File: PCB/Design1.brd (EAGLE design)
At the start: 73 x 41 mm, 41 parts, among them J1 FTDI, U1 ATMEGA2560AU, Y1 16MHZ

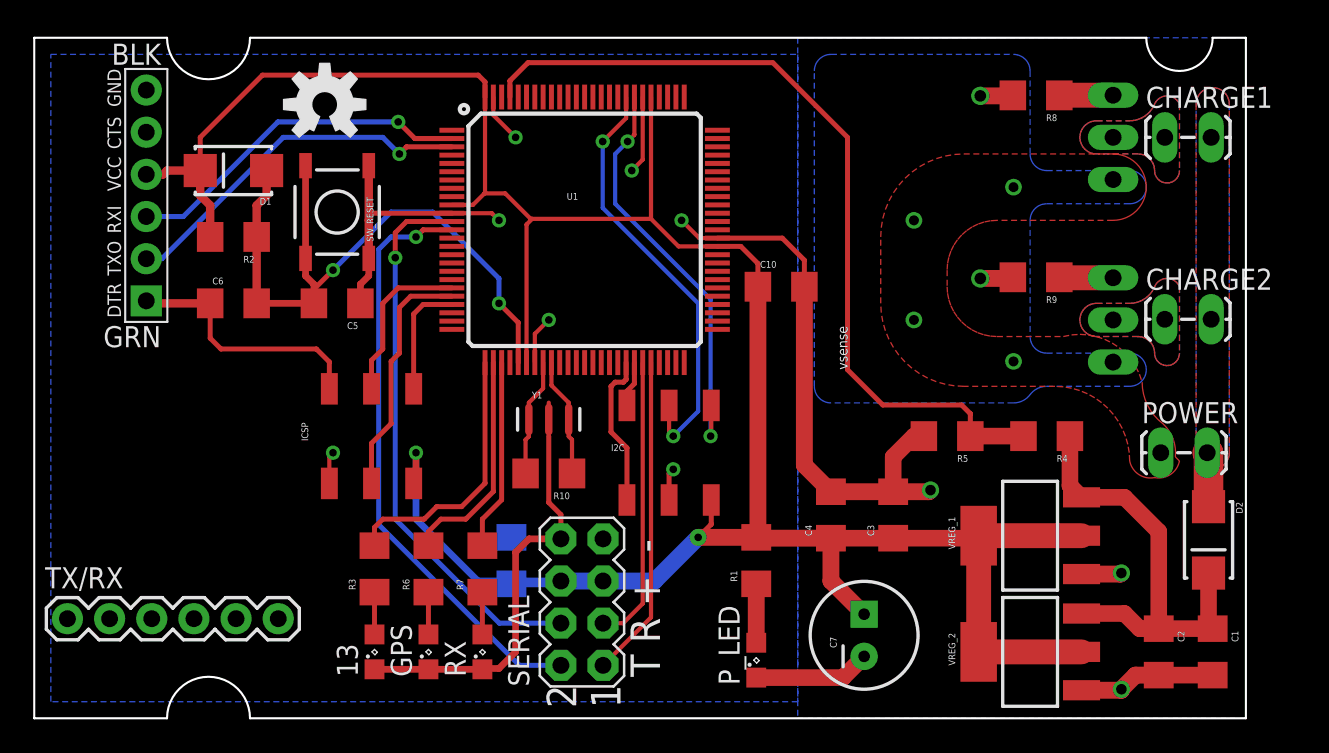
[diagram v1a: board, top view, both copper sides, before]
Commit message: Removed 1x 5v regulator; relabeling
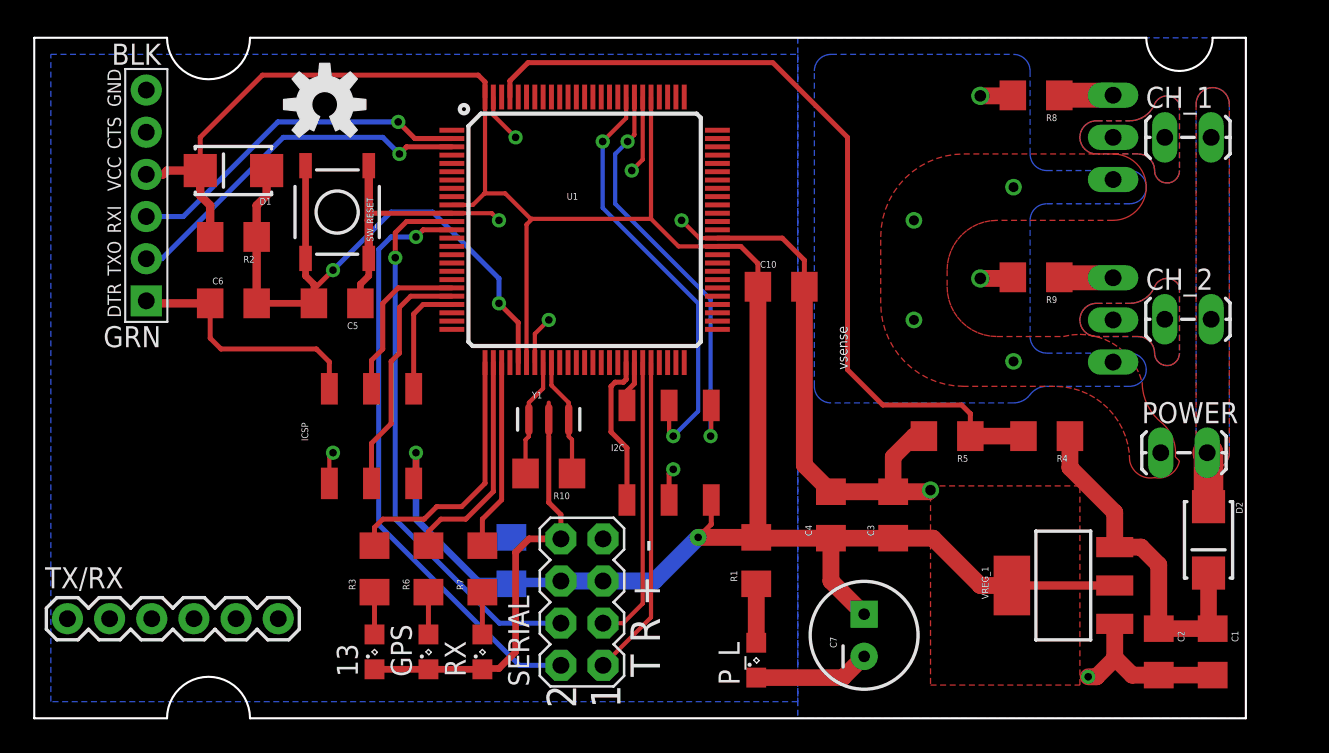
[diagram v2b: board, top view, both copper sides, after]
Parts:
- removed VREG_2: (no value), SparkFun-PowerIC:SOT223
- P_L: value red -> (none)
- moved VREG_1 3.61 mm to (62.0, 8.00)
- renumbered CHARGE1 to CH_1, CHARGE2 to CH_2, P_LED to P_L
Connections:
- net 5V: no longer VREG_2.2, VREG_2.4
- net GND: no longer VREG_2.1
- net VIN_RECTIFIED: no longer VREG_2.3
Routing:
- net 5V: track 161.3 -> 151.2 mm
- net VIN_RECTIFIED: track 27.1 -> 21.5 mm
- net GND: track 111.2 -> 111.0 mm, vias 16 -> 15
- added copper zone on layer 1, net 5V
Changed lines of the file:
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@@
 <text x="35.32" y="0.62" size="1.778" layer="21" rot="R90">2
 1</text>
-<dimension x1="74" y1="41" x2="74" y2="0" x3="78" y3="20.5" textsize="1.778" layer="51" visible="yes"/>
-<dimension x1="0" y1="42" x2="73" y2="42" x3="36.5" y3="43" textsize="1.778" layer="51" visible="yes"/>
 <wire x1="46" y1="41" x2="46" y2="18" width="0.254" layer="22"/>
 <wire x1="46" y1="18" x2="65" y2="18" width="0.254" layer="22"/>
@@
 <attribute name="VALUE" x="23.822" y="17.408" size="0.4064" layer="27" rot="R180"/>
 </element>
-<element name="P_LED" library="led" package="SML0805" value="red" x="43.5" y="3.5" rot="R90"/>
+<element name="P_L" library="led" package="SML0805" value="" x="43.5" y="3.5" rot="R90"/>
 <element name="R1" library="SparkFun-Resistors" package="1206" value="100Ω" x="43.5" y="9.5" rot="R90"/>
 <element name="GPS" library="led" package="SML0805" value="" x="23.75" y="4" rot="R90"/>
@@
 <element name="R8" library="SparkFun-Resistors" package="1206" value="10KΩ" x="60.36" y="37.53" rot="R180"/>
 <element name="R9" library="SparkFun-Resistors" package="1206" value="10KΩ" x="60.36" y="26.57" rot="R180"/>
-<element name="CHARGE1" library="SparkFun-Connectors" package="1X02_LOCK_LONGPADS" value="" x="68.24" y="35"/>
-<element name="CHARGE2" library="SparkFun-Connectors" package="1X02_LOCK_LONGPADS" value="" x="68.24" y="24.04"/>
-<element name="VREG_1" library="SparkFun-PowerIC" package="SOT223" value="" x="60" y="11" rot="R90">
-<attribute name="PROD_ID" value="VREG-08170" x="60" y="11" size="1.778" layer="27" rot="R90" display="off"/>
-</element>
-<element name="VREG_2" library="SparkFun-PowerIC" package="SOT223" value="" x="60" y="4" rot="R90">
-<attribute name="PROD_ID" value="VREG-08170" x="60" y="4" size="1.778" layer="27" rot="R90" display="off"/>
+<element name="CH_1" library="SparkFun-Connectors" package="1X02_LOCK_LONGPADS" value="" x="68.24" y="35"/>
+<element name="CH_2" library="SparkFun-Connectors" package="1X02_LOCK_LONGPADS" value="" x="68.24" y="24.04"/>
+<element name="VREG_1" library="SparkFun-PowerIC" package="SOT223" value="" x="62" y="8" rot="R90">
+<attribute name="PROD_ID" value="VREG-08170" x="62" y="8" size="1.778" layer="27" rot="R90" display="off"/>
 </element>
 <element name="C7" library="SparkFun-Capacitors" package="CPOL-RADIAL-100UF-25V" value="470uF" x="50" y="5" rot="R90"/>
@@
 <contactref element="R5" pad="2"/>
 <contactref element="ICSP" pad="6"/>
-<contactref element="P_LED" pad="C"/>
+<contactref element="P_L" pad="C"/>
 <contactref element="RX" pad="C"/>
 <contactref element="GPS" pad="C"/>
@@
 <contactref element="R8" pad="2"/>
 <contactref element="R9" pad="2"/>
-<contactref element="VREG_2" pad="1"/>
 <contactref element="VREG_1" pad="1"/>
 <contactref element="C7" pad="2"/>
@@
 <vertex x="73" y="41"/>
 </polygon>
-<via x="65.5" y="8.75" extent="1-16" drill="0.635"/>
-<via x="65.5" y="1.75" extent="1-16" drill="0.635"/>
 <wire x1="67.75" y1="2.6" x2="71" y2="2.6" width="1" layer="1"/>
 <wire x1="51.75" y1="13.65" x2="51.75" y2="15.75" width="1" layer="1"/>
@@
 <wire x1="53" y1="17" x2="53.6" y2="17" width="1" layer="1"/>
 <via x="54" y="13.75" extent="1-16" drill="0.635"/>
-<wire x1="63.0988" y1="1.6886" x2="65.5" y2="1.6886" width="1.016" layer="1"/>
-<wire x1="65.5" y1="1.6886" x2="65.5" y2="1.75" width="1.016" layer="1"/>
-<wire x1="67.75" y1="2.6" x2="66.35" y2="2.6" width="1.016" layer="1"/>
-<wire x1="66.35" y1="2.6" x2="65.5" y2="1.75" width="1.016" layer="1"/>
-<wire x1="63.0988" y1="8.6886" x2="65.4386" y2="8.6886" width="1.016" layer="1"/>
-<wire x1="65.4386" y1="8.6886" x2="65.5" y2="8.75" width="1.016" layer="1"/>
 <wire x1="51.75" y1="13.65" x2="53.9" y2="13.65" width="1.016" layer="1"/>
 <wire x1="53.9" y1="13.65" x2="54" y2="13.75" width="1.016" layer="1"/>
@@
 <wire x1="29" y1="10" x2="29.81" y2="10.81" width="0.4064" layer="1"/>
 <wire x1="29.81" y1="10.81" x2="31.73" y2="10.81" width="0.4064" layer="1"/>
+<wire x1="67.75" y1="2.6" x2="66.15" y2="2.6" width="1.016" layer="1"/>
+<wire x1="66.15" y1="2.6" x2="65.125" y2="3.625" width="1.016" layer="1"/>
+<wire x1="65.125" y1="3.625" x2="65.0988" y2="3.6512" width="1.016" layer="1"/>
+<wire x1="65.0988" y1="3.6512" x2="65.0988" y2="5.6886" width="1.016" layer="1"/>
+<via x="63.5" y="2.5" extent="1-16" drill="0.4572"/>
+<wire x1="63.5" y1="2.5" x2="64" y2="2.5" width="1.016" layer="1"/>
+<wire x1="64" y1="2.5" x2="65.125" y2="3.625" width="1.016" layer="1"/>
 </signal>
 <signal name="RESET">
@@
 <contactref element="VREG_1" pad="2"/>
 <contactref element="VREG_1" pad="4"/>
-<contactref element="VREG_2" pad="2"/>
-<contactref element="VREG_2" pad="4"/>
 <contactref element="C7" pad="1"/>
-<wire x1="63.0988" y1="11" x2="56.901" y2="11" width="1.5" layer="1"/>
-<wire x1="63.0988" y1="4" x2="56.901" y2="4" width="1.5" layer="1"/>
-<wire x1="56.901" y1="11" x2="56.901" y2="4" width="1.5" layer="1"/>
 <wire x1="48" y1="10.85" x2="51.75" y2="10.85" width="1" layer="1"/>
-<wire x1="51.75" y1="10.85" x2="56.751" y2="10.85" width="1" layer="1"/>
-<wire x1="56.751" y1="10.85" x2="56.901" y2="11" width="1" layer="1"/>
 <contactref element="C9" pad="1"/>
 <contactref element="C10" pad="1"/>
@@
 <wire x1="28.75" y1="8.1" x2="31.56" y2="8.1" width="0.4064" layer="16"/>
 <wire x1="31.56" y1="8.1" x2="31.73" y2="8.27" width="0.4064" layer="16"/>
+<polygon width="0.3" layer="1" isolate="1.016">
+<vertex x="54" y="14"/>
+<vertex x="54" y="2"/>
+<vertex x="63" y="2"/>
+<vertex x="63" y="14"/>
+</polygon>
+<wire x1="51.75" y1="10.85" x2="54.15" y2="10.85" width="1.016" layer="1"/>
+<wire x1="54.15" y1="10.85" x2="57" y2="8" width="1.016" layer="1"/>
+<wire x1="57" y1="8" x2="58.901" y2="8" width="1.016" layer="1"/>
+<wire x1="65.0988" y1="8" x2="58.901" y2="8" width="0.508" layer="1"/>
 </signal>
 <signal name="TX1">
@@
 <contactref element="POWER" pad="2"/>
 <contactref element="D2" pad="A"/>
-<contactref element="CHARGE2" pad="2"/>
-<contactref element="CHARGE1" pad="2"/>
+<contactref element="CH_2" pad="2"/>
+<contactref element="CH_1" pad="2"/>
 <polygon width="0.254" layer="16" isolate="0.254" thermals="no">
 <vertex x="71" y="38" curve="-90"/>
@@
 </signal>
 <signal name="N$2">
-<contactref element="P_LED" pad="A"/>
+<contactref element="P_L" pad="A"/>
 <contactref element="R1" pad="1"/>
 <wire x1="43.5" y1="4.55" x2="43.5" y2="8.1" width="1.016" layer="1"/>
@@
 <signal name="MOS1">
 <contactref element="MOS1" pad="2"/>
-<contactref element="CHARGE1" pad="1"/>
+<contactref element="CH_1" pad="1"/>
 <polygon width="0.254" layer="16" thermals="no">
 <vertex x="64" y="36"/>
@@
 <signal name="MOS2">
 <contactref element="MOS2" pad="2"/>
-<contactref element="CHARGE2" pad="1"/>
+<contactref element="CH_2" pad="1"/>
 <polygon width="0.254" layer="1" thermals="no">
 <vertex x="64" y="25"/>
@@
 <contactref element="C1" pad="1"/>
 <contactref element="VREG_1" pad="3"/>
-<contactref element="VREG_2" pad="3"/>
 <wire x1="71" y1="5.4" x2="67.75" y2="5.4" width="1" layer="1"/>
 <wire x1="71" y1="5.4" x2="70.75" y2="5.65" width="1" layer="1"/>
 <wire x1="70.75" y1="5.65" x2="70.75" y2="8.75" width="1" layer="1"/>
-<wire x1="63.0988" y1="13.3114" x2="65.6886" y2="13.3114" width="1" layer="1"/>
-<wire x1="65.6886" y1="13.3114" x2="67.75" y2="11.25" width="1" layer="1"/>
-<wire x1="67.75" y1="11.25" x2="67.75" y2="5.4" width="1" layer="1"/>
-<wire x1="63.0988" y1="6.3114" x2="65.6886" y2="6.3114" width="1" layer="1"/>
-<wire x1="65.6886" y1="6.3114" x2="66.6" y2="5.4" width="1" layer="1"/>
-<wire x1="66.6" y1="5.4" x2="67.75" y2="5.4" width="1" layer="1"/>
-<wire x1="63.0988" y1="13.3114" x2="62.4" y2="14.0102" width="1" layer="1"/>
-<wire x1="62.4" y1="14.0102" x2="62.4" y2="17" width="1" layer="1"/>
+<wire x1="67.75" y1="5.4" x2="67.75" y2="9.25" width="1.016" layer="1"/>
+<wire x1="67.75" y1="9.25" x2="66.6886" y2="10.3114" width="1.016" layer="1"/>
+<wire x1="66.6886" y1="10.3114" x2="65.0988" y2="10.3114" width="1.016" layer="1"/>
+<wire x1="62.4" y1="17" x2="62.4" y2="15.1" width="1.016" layer="1"/>
+<wire x1="62.4" y1="15.1" x2="65.0988" y2="12.4012" width="1.016" layer="1"/>
+<wire x1="65.0988" y1="12.4012" x2="65.0988" y2="10.3114" width="1.016" layer="1"/>
 </signal>
 <signal name="N$5">

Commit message: Labeling Cleanup
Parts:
- ATMEGA2560AU: value ATMEGA2560AU -> (none)
- renumbered U1 to ATMEGA2560AU, VREG_1 to VREG
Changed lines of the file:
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@@
 </autorouter>
 <elements>
-<element name="U1" library="SparkFun-DigitalIC" package="TQFP100" value="ATMEGA2560AU" x="33.16" y="29.43" locked="yes" smashed="yes">
+<element name="ATMEGA2560AU" library="SparkFun-DigitalIC" package="TQFP100" value="" x="33.16" y="29.43" locked="yes">
 <attribute name="PROD_ID" value="IC-10040" x="33.16" y="29.43" size="1.778" layer="27" display="off"/>
-<attribute name="NAME" x="32.08" y="31.24" size="0.4064" layer="25"/>
-<attribute name="VALUE" x="31.08" y="26.62" size="0.4064" layer="27"/>
 </element>
 <element name="J1" library="SparkFun-Connectors" package="FTDI_DEVICE_SIDE" value="FTDI" x="6.75" y="31.5" locked="yes" rot="R90"/>
@@
 <element name="CH_1" library="SparkFun-Connectors" package="1X02_LOCK_LONGPADS" value="" x="68.24" y="35"/>
 <element name="CH_2" library="SparkFun-Connectors" package="1X02_LOCK_LONGPADS" value="" x="68.24" y="24.04"/>
-<element name="VREG_1" library="SparkFun-PowerIC" package="SOT223" value="" x="62" y="8" rot="R90">
+<element name="VREG" library="SparkFun-PowerIC" package="SOT223" value="" x="62" y="8" rot="R90">
 <attribute name="PROD_ID" value="VREG-08170" x="62" y="8" size="1.778" layer="27" rot="R90" display="off"/>
 </element>
@@
 <signals>
 <signal name="GND">
-<contactref element="U1" pad="81"/>
-<contactref element="U1" pad="62"/>
+<contactref element="ATMEGA2560AU" pad="81"/>
+<contactref element="ATMEGA2560AU" pad="62"/>
 <contactref element="J1" pad="P$6"/>
 <contactref element="J1" pad="P$5"/>
 <contactref element="13" pad="C"/>
 <contactref element="POWER" pad="1"/>
-<contactref element="U1" pad="32"/>
-<contactref element="U1" pad="11"/>
-<contactref element="U1" pad="99"/>
+<contactref element="ATMEGA2560AU" pad="32"/>
+<contactref element="ATMEGA2560AU" pad="11"/>
+<contactref element="ATMEGA2560AU" pad="99"/>
 <contactref element="C5" pad="1"/>
 <contactref element="C1" pad="2"/>
@@
 <contactref element="R8" pad="2"/>
 <contactref element="R9" pad="2"/>
-<contactref element="VREG_1" pad="1"/>
+<contactref element="VREG" pad="1"/>
 <contactref element="C7" pad="2"/>
 <polygon width="0.254" layer="16" isolate="1.016" thermals="no" rank="2">
@@
 <contactref element="SW_RESET" pad="3"/>
 <contactref element="SW_RESET" pad="4"/>
-<contactref element="U1" pad="30"/>
+<contactref element="ATMEGA2560AU" pad="30"/>
 <wire x1="13.4" y1="25" x2="13.4" y2="29" width="0.508" layer="1"/>
 <wire x1="13.4" y1="29" x2="13.4" y2="30.9" width="0.508" layer="1"/>
@@
 <signal name="LED_13">
 <contactref element="R3" pad="2"/>
-<contactref element="U1" pad="26"/>
+<contactref element="ATMEGA2560AU" pad="26"/>
 <wire x1="27.16" y1="21.43" x2="27.16" y2="14.16" width="0.3" layer="1"/>
 <wire x1="27.16" y1="14.16" x2="25.75" y2="12.75" width="0.3" layer="1"/>
@@
 </signal>
 <signal name="TX0">
-<contactref element="U1" pad="3"/>
+<contactref element="ATMEGA2560AU" pad="3"/>
 <contactref element="J1" pad="P$2"/>
 <wire x1="6.75" y1="27.69" x2="7.69" y2="27.69" width="0.3048" layer="16"/>
@@
 </signal>
 <signal name="RX0">
-<contactref element="U1" pad="2"/>
+<contactref element="ATMEGA2560AU" pad="2"/>
 <contactref element="J1" pad="P$3"/>
 <via x="21.93" y="35.93" extent="1-16" drill="0.4572"/>
@@
 </signal>
 <signal name="5V">
-<contactref element="U1" pad="10"/>
-<contactref element="U1" pad="80"/>
-<contactref element="U1" pad="61"/>
-<contactref element="U1" pad="31"/>
-<contactref element="U1" pad="100"/>
+<contactref element="ATMEGA2560AU" pad="10"/>
+<contactref element="ATMEGA2560AU" pad="80"/>
+<contactref element="ATMEGA2560AU" pad="61"/>
+<contactref element="ATMEGA2560AU" pad="31"/>
+<contactref element="ATMEGA2560AU" pad="100"/>
 <contactref element="J1" pad="P$4"/>
 <contactref element="C4" pad="1"/>
@@
 <contactref element="ICSP" pad="2"/>
 <contactref element="R1" pad="2"/>
-<contactref element="VREG_1" pad="2"/>
-<contactref element="VREG_1" pad="4"/>
+<contactref element="VREG" pad="2"/>
+<contactref element="VREG" pad="4"/>
 <contactref element="C7" pad="1"/>
 <wire x1="48" y1="10.85" x2="51.75" y2="10.85" width="1" layer="1"/>
@@
 </signal>
 <signal name="TX1">
-<contactref element="U1" pad="46"/>
+<contactref element="ATMEGA2560AU" pad="46"/>
 <contactref element="SERIAL" pad="1"/>
 <wire x1="37.16" y1="21.43" x2="37.16" y2="6.08" width="0.254" layer="1"/>
@@
 </signal>
 <signal name="RX1">
-<contactref element="U1" pad="45"/>
+<contactref element="ATMEGA2560AU" pad="45"/>
 <contactref element="SERIAL" pad="3"/>
 <wire x1="36.66" y1="21.43" x2="36.66" y2="6.91" width="0.254" layer="1"/>
@@
 </signal>
 <signal name="TX2">
-<contactref element="U1" pad="13"/>
+<contactref element="ATMEGA2560AU" pad="13"/>
 <contactref element="SERIAL" pad="2"/>
 <wire x1="20.75" y1="11.67" x2="20.75" y2="28.25" width="0.3" layer="16"/>
@@
 </signal>
 <signal name="RX2">
-<contactref element="U1" pad="12"/>
+<contactref element="ATMEGA2560AU" pad="12"/>
 <contactref element="SERIAL" pad="4"/>
 <wire x1="21.75" y1="12" x2="21.75" y2="27.75" width="0.3" layer="16"/>
@@
 <contactref element="R5" pad="1"/>
 <wire x1="59.6" y1="17" x2="56.4" y2="17" width="1" layer="1"/>
-<contactref element="U1" pad="97"/>
+<contactref element="ATMEGA2560AU" pad="97"/>
 <wire x1="56.4" y1="17" x2="56.4" y2="18.35" width="0.3048" layer="1"/>
 <wire x1="56.4" y1="18.35" x2="55.875" y2="18.875" width="0.3048" layer="1"/>
@@
 <signal name="SCK">
 <contactref element="ICSP" pad="3"/>
-<contactref element="U1" pad="20"/>
+<contactref element="ATMEGA2560AU" pad="20"/>
 <wire x1="25.16" y1="25.93" x2="21.93" y2="25.93" width="0.3" layer="1"/>
 <wire x1="21" y1="25" x2="21" y2="22.25" width="0.3" layer="1"/>
@@
 <signal name="MISO">
 <contactref element="ICSP" pad="1"/>
-<contactref element="U1" pad="22"/>
+<contactref element="ATMEGA2560AU" pad="22"/>
 <wire x1="25.16" y1="24.93" x2="23.43" y2="24.93" width="0.3" layer="1"/>
 <wire x1="23.43" y1="24.93" x2="22.86" y2="24.36" width="0.3" layer="1"/>
@@
 <signal name="MOSI">
 <contactref element="ICSP" pad="4"/>
-<contactref element="U1" pad="21"/>
+<contactref element="ATMEGA2560AU" pad="21"/>
 <wire x1="25.16" y1="25.43" x2="22.68" y2="25.43" width="0.3" layer="1"/>
 <wire x1="21.5" y1="17.75" x2="20.32" y2="16.57" width="0.3" layer="1"/>
@@
 <signal name="LED_GPS">
 <contactref element="R6" pad="2"/>
-<contactref element="U1" pad="27"/>
+<contactref element="ATMEGA2560AU" pad="27"/>
 <wire x1="27.66" y1="21.43" x2="27.66" y2="13.66" width="0.3" layer="1"/>
 <wire x1="27.66" y1="13.66" x2="26" y2="12" width="0.3" layer="1"/>
@@
 <signal name="LED_RX">
 <contactref element="R7" pad="2"/>
-<contactref element="U1" pad="28"/>
+<contactref element="ATMEGA2560AU" pad="28"/>
 <wire x1="28.16" y1="21.43" x2="28.16" y2="13.16" width="0.3" layer="1"/>
 <wire x1="28.16" y1="13.16" x2="27" y2="12" width="0.3" layer="1"/>
@@
 <contactref element="C2" pad="1"/>
 <contactref element="C1" pad="1"/>
-<contactref element="VREG_1" pad="3"/>
+<contactref element="VREG" pad="3"/>
 <wire x1="71" y1="5.4" x2="67.75" y2="5.4" width="1" layer="1"/>
 <wire x1="71" y1="5.4" x2="70.75" y2="5.65" width="1" layer="1"/>
@@
 <signal name="XTAL2">
 <contactref element="Y1" pad="1"/>
-<contactref element="U1" pad="33"/>
+<contactref element="ATMEGA2560AU" pad="33"/>
 <contactref element="R10" pad="2"/>
 <wire x1="29.8" y1="16.984" x2="29.6" y2="16.784" width="0.254" layer="1"/>
@@
 <signal name="XTAL1">
 <contactref element="Y1" pad="3"/>
-<contactref element="U1" pad="34"/>
+<contactref element="ATMEGA2560AU" pad="34"/>
 <contactref element="R10" pad="1"/>
 <wire x1="32.2" y1="16.984" x2="32.4" y2="16.784" width="0.254" layer="1"/>
@@
 </signal>
 <signal name="SDA">
-<contactref element="U1" pad="44"/>
+<contactref element="ATMEGA2560AU" pad="44"/>
 <contactref element="I2C" pad="2"/>
 <wire x1="36.16" y1="21.43" x2="36.16" y2="20.16" width="0.3048" layer="1"/>
@@
 </signal>
 <signal name="SCL">
-<contactref element="U1" pad="43"/>
+<contactref element="ATMEGA2560AU" pad="43"/>
 <contactref element="I2C" pad="1"/>
 <wire x1="35.66" y1="21.43" x2="35.66" y2="20.41" width="0.3048" layer="1"/>
@@
 </signal>
 <signal name="ADC14">
-<contactref element="U1" pad="83"/>
+<contactref element="ATMEGA2560AU" pad="83"/>
 <contactref element="I2C" pad="4"/>
 <wire x1="35.66" y1="37.43" x2="35.66" y2="36.16" width="0.254" layer="1"/>
@@
 </signal>
 <signal name="ADC15">
-<contactref element="U1" pad="82"/>
+<contactref element="ATMEGA2560AU" pad="82"/>
 <contactref element="I2C" pad="6"/>
 <wire x1="36.16" y1="37.43" x2="36.16" y2="35.16" width="0.254" layer="1"/>
